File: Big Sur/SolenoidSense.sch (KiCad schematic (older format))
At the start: 46 parts, among them U5 LM324DRG4, U6 LM324DRG4, U7 LM324DRG4

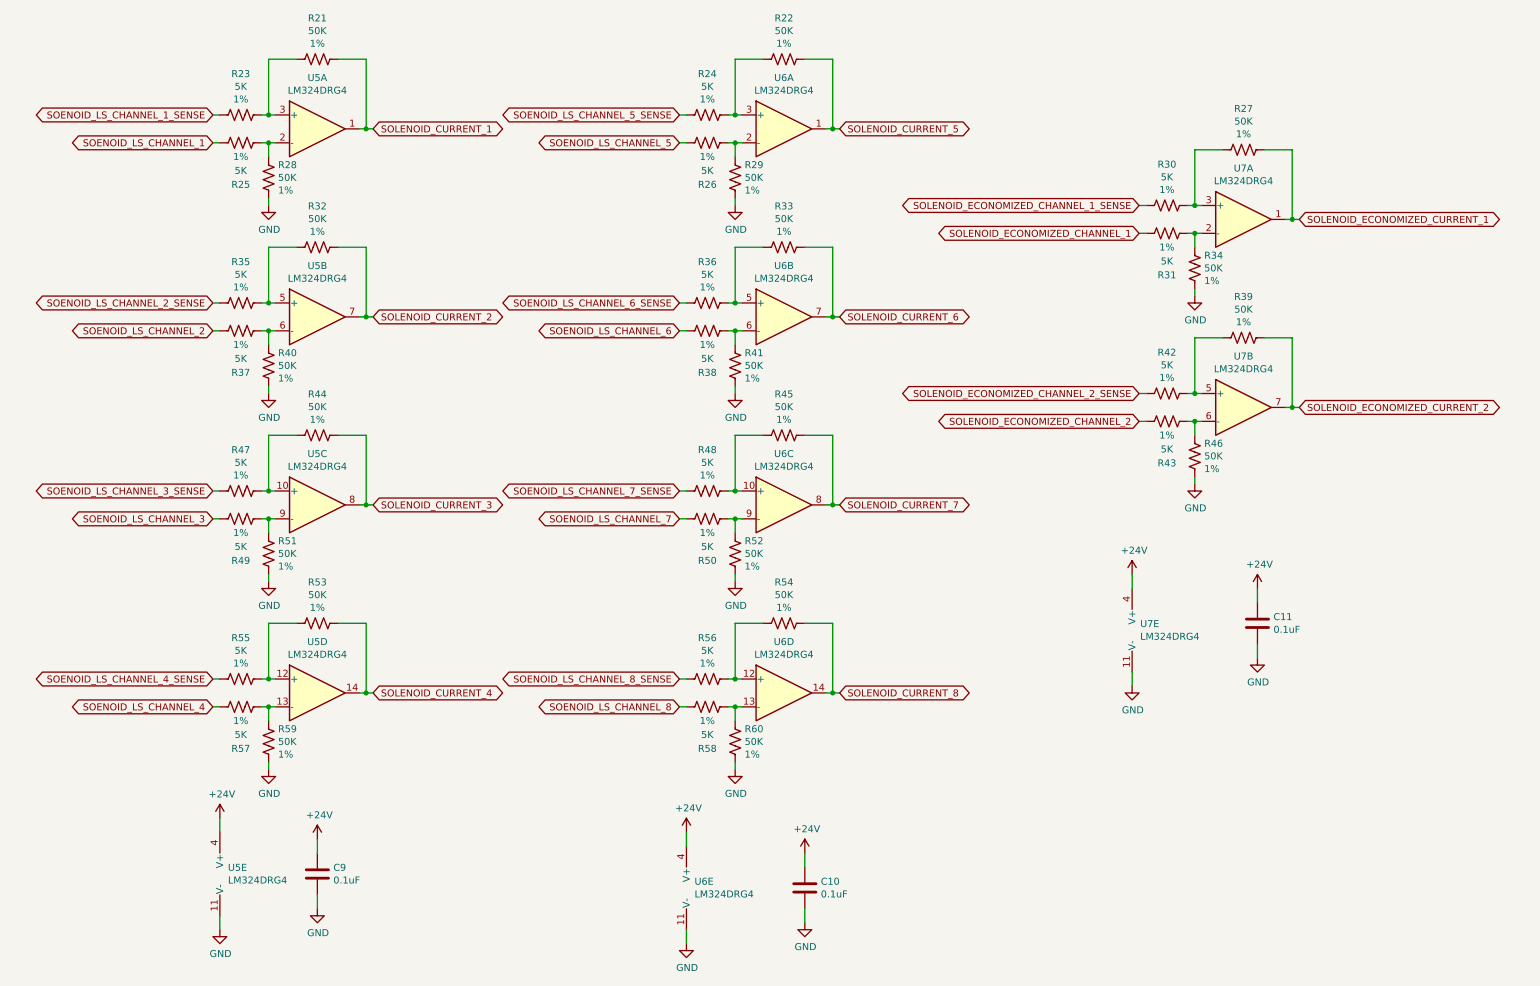
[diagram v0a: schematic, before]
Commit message: Updated current sense, second pump driver, solenoid connectors
-Current sense now uses current sense ICs, connected to Paraduino ADC pins.
-Added second pump driver.
-Connected outputs with XT30 connectors.
-Still need some Paraduino connections, inverter driver, footprints.
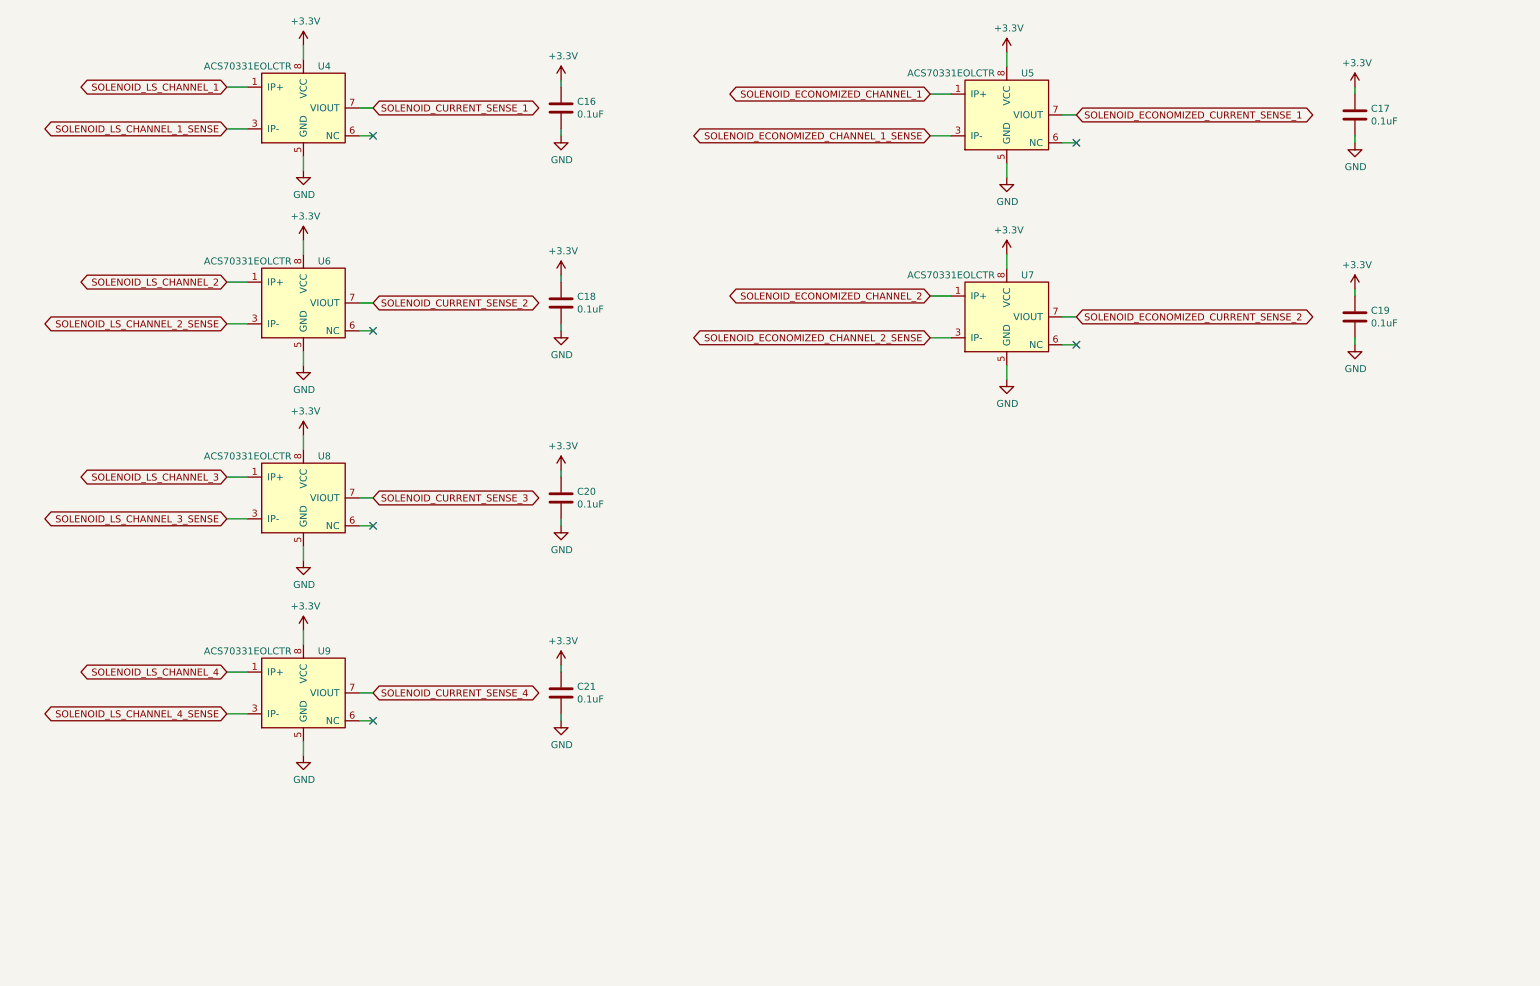
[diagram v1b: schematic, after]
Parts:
- removed C10, C11, C9: 0.1uF, symbol Device:C
- removed R21, R22, R27, R28, R29, R32, R33, R34, R39, R40, R41, R44, R45, R46, R51, R52, R53, R54, R59, R60: 50K, symbol Device:R_US
- removed R23, R24, R25, R26, R30, R31, R35, R36, R37, R38, R42, R43, R47, R48, R49, R50, R55, R56, R57, R58: 5K, symbol Device:R_US
- removed U5, U6, U7: LM324DRG4, symbol Amplifier_Operational:LM324
- added C16, C17, C18, C19, C20, C21: 0.1uF, symbol Device:C
- added U4, U5, U6, U7, U8, U9: ACS70331EOLCTR, Big Sur:Allegro_SOIC_6.2x5.0mm_P1.27mm, symbol BigSurLib:ACS70331EOLCTR
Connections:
- net GND: now also C16.2, C17.2, C18.2, C19.2, C20.2, C21.2, U4.5 (GND), U5.5 (GND), U6.5 (GND), U7.5 (GND), U8.5 (GND), U9.5 (GND)
- net SOLENOID_ECONOMIZED_CHANNEL_1: now also U5.1 (IP+)
- net SOLENOID_ECONOMIZED_CHANNEL_1_SENSE: now also U5.3 (IP-)
- net SOLENOID_ECONOMIZED_CHANNEL_2: now also U7.1 (IP+)
- net SOLENOID_ECONOMIZED_CHANNEL_2_SENSE: now also U7.3 (IP-)
- new net +3V3: C16.1, C17.1, C18.1, C19.1, C20.1, C21.1, U4.8 (VCC), U5.8 (VCC), U6.8 (VCC), U7.8 (VCC), U8.8 (VCC), U9.8 (VCC)
- new net SOLENOID_CURRENT_SENSE_1: U4.7 (VIOUT)
- new net SOLENOID_CURRENT_SENSE_2: U6.7 (VIOUT)
- new net SOLENOID_CURRENT_SENSE_3: U8.7 (VIOUT)
- new net SOLENOID_CURRENT_SENSE_4: U9.7 (VIOUT)
- new net SOLENOID_ECONOMIZED_CURRENT_SENSE_1: U5.7 (VIOUT)
- new net SOLENOID_ECONOMIZED_CURRENT_SENSE_2: U7.7 (VIOUT)
- new net SOLENOID_LS_CHANNEL_1: U4.1 (IP+)
- new net SOLENOID_LS_CHANNEL_1_SENSE: U4.3 (IP-)
- new net SOLENOID_LS_CHANNEL_2: U6.1 (IP+)
- new net SOLENOID_LS_CHANNEL_2_SENSE: U6.3 (IP-)
- new net SOLENOID_LS_CHANNEL_3: U8.1 (IP+)
- new net SOLENOID_LS_CHANNEL_3_SENSE: U8.3 (IP-)
- new net SOLENOID_LS_CHANNEL_4: U9.1 (IP+)
- new net SOLENOID_LS_CHANNEL_4_SENSE: U9.3 (IP-)
- no-connect marks 0 -> 6

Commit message: Removed Inverter
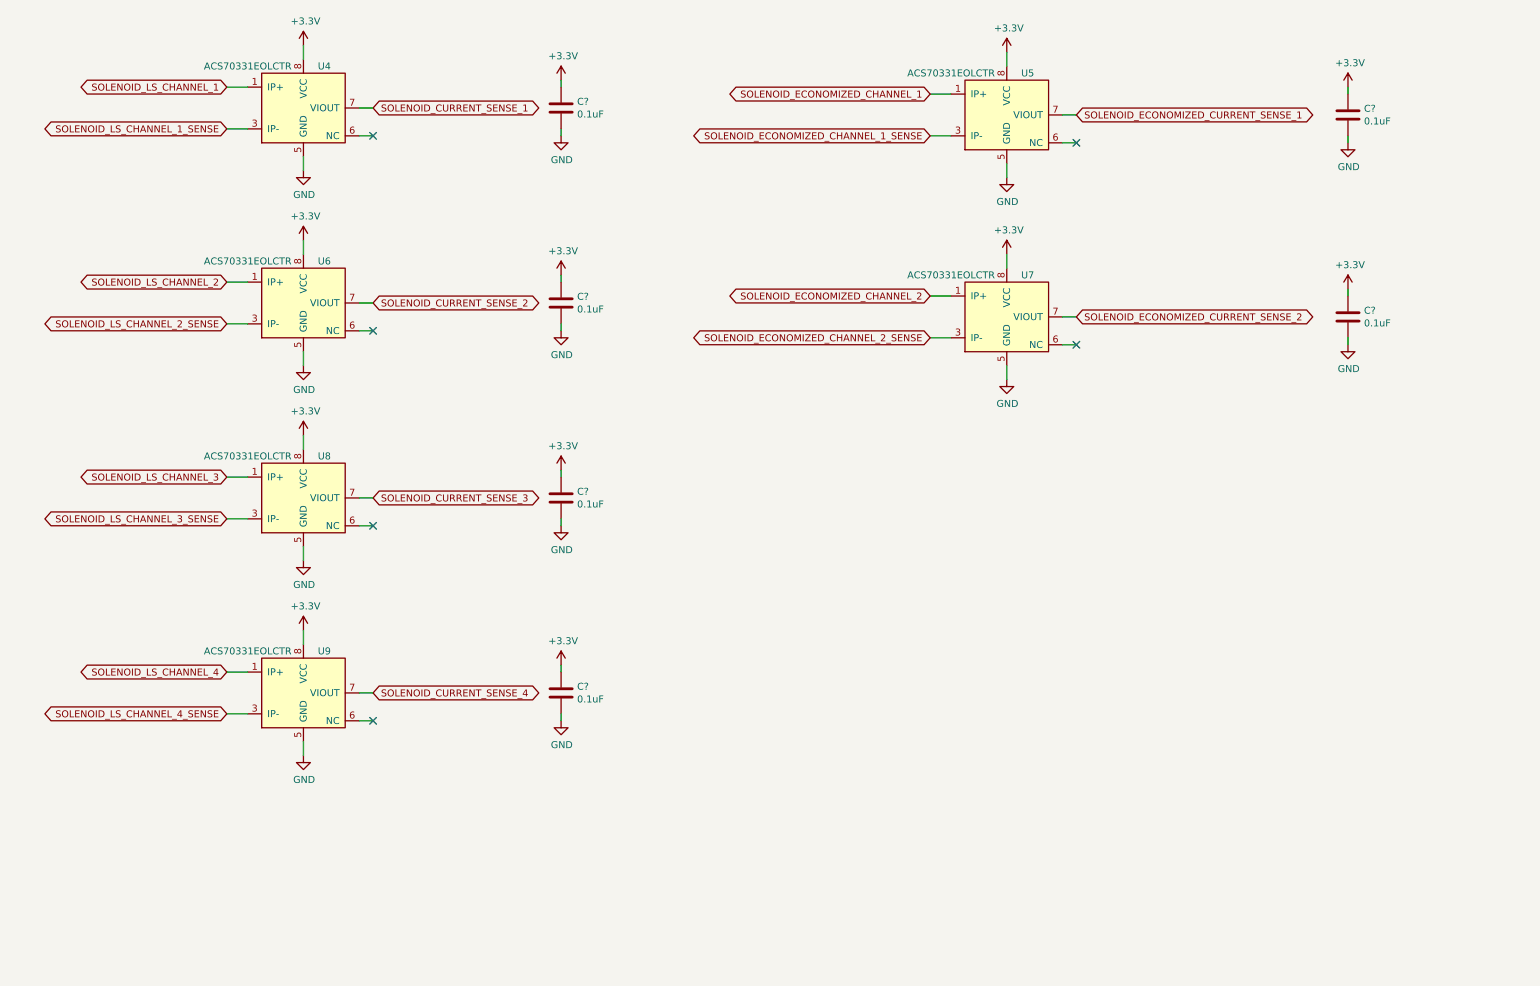
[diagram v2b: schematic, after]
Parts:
- removed C16, C17, C18, C19, C20, C21: 0.1uF, symbol Device:C
- added C? (x6): 0.1uF, Capacitor_SMD:C_0603_1608Metric_Pad1.05x0.95mm_HandSolder, symbol Device:C
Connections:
- net +3V3: now also C?.1, C?.1, C?.1, C?.1, C?.1, C?.1
- net GND: now also C?.2, C?.2, C?.2, C?.2, C?.2, C?.2
